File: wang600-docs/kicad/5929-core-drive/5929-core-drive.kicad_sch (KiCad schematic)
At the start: 29 parts, among them U17 7400

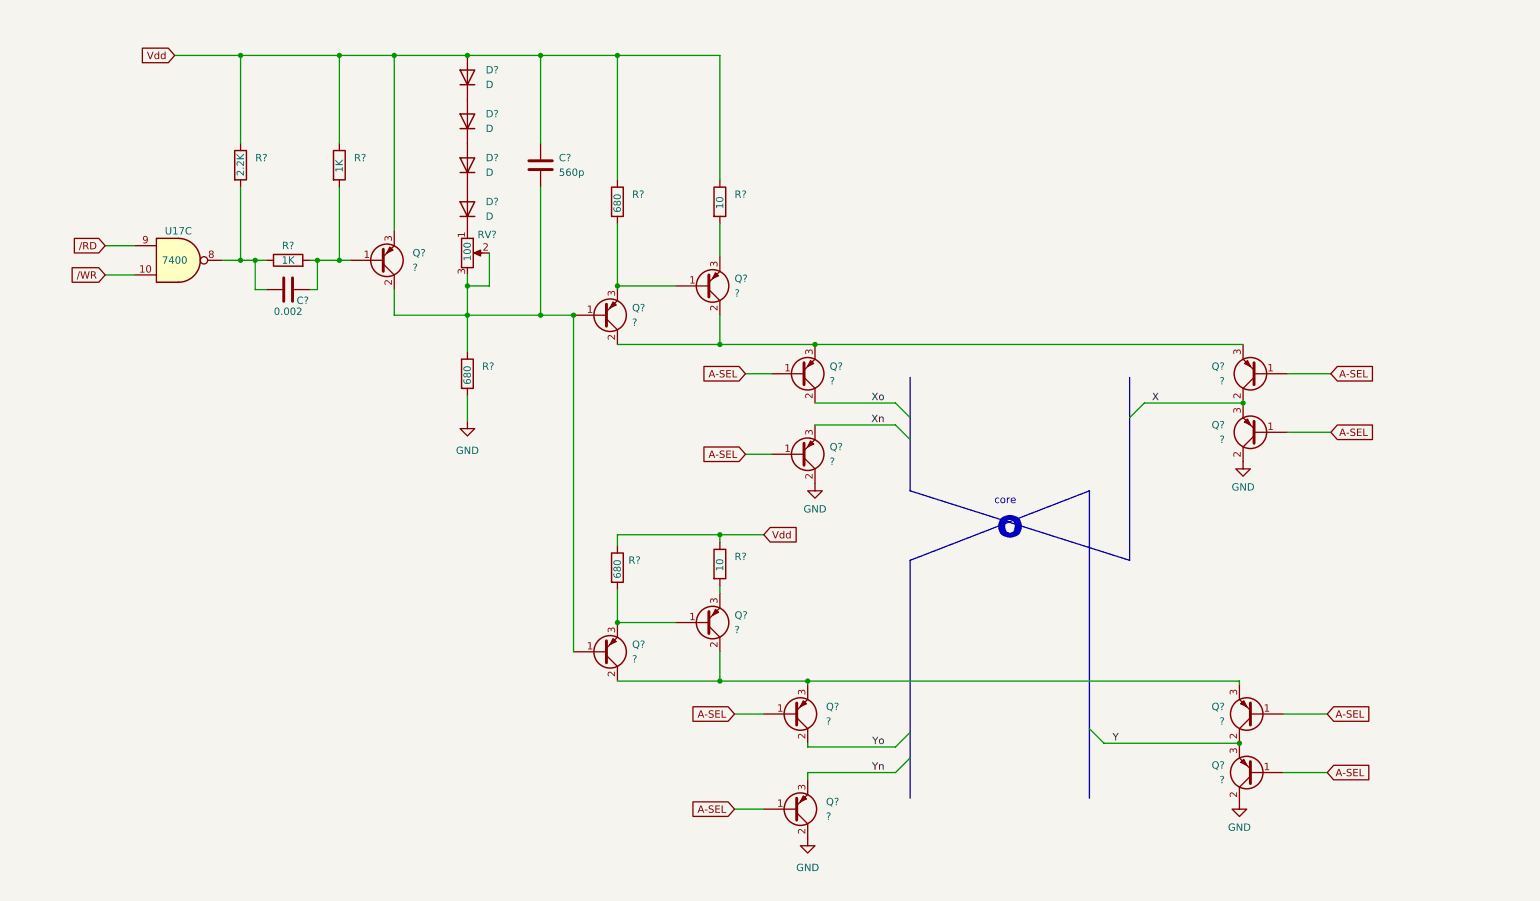
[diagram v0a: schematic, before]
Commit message: add transistor data to schematic
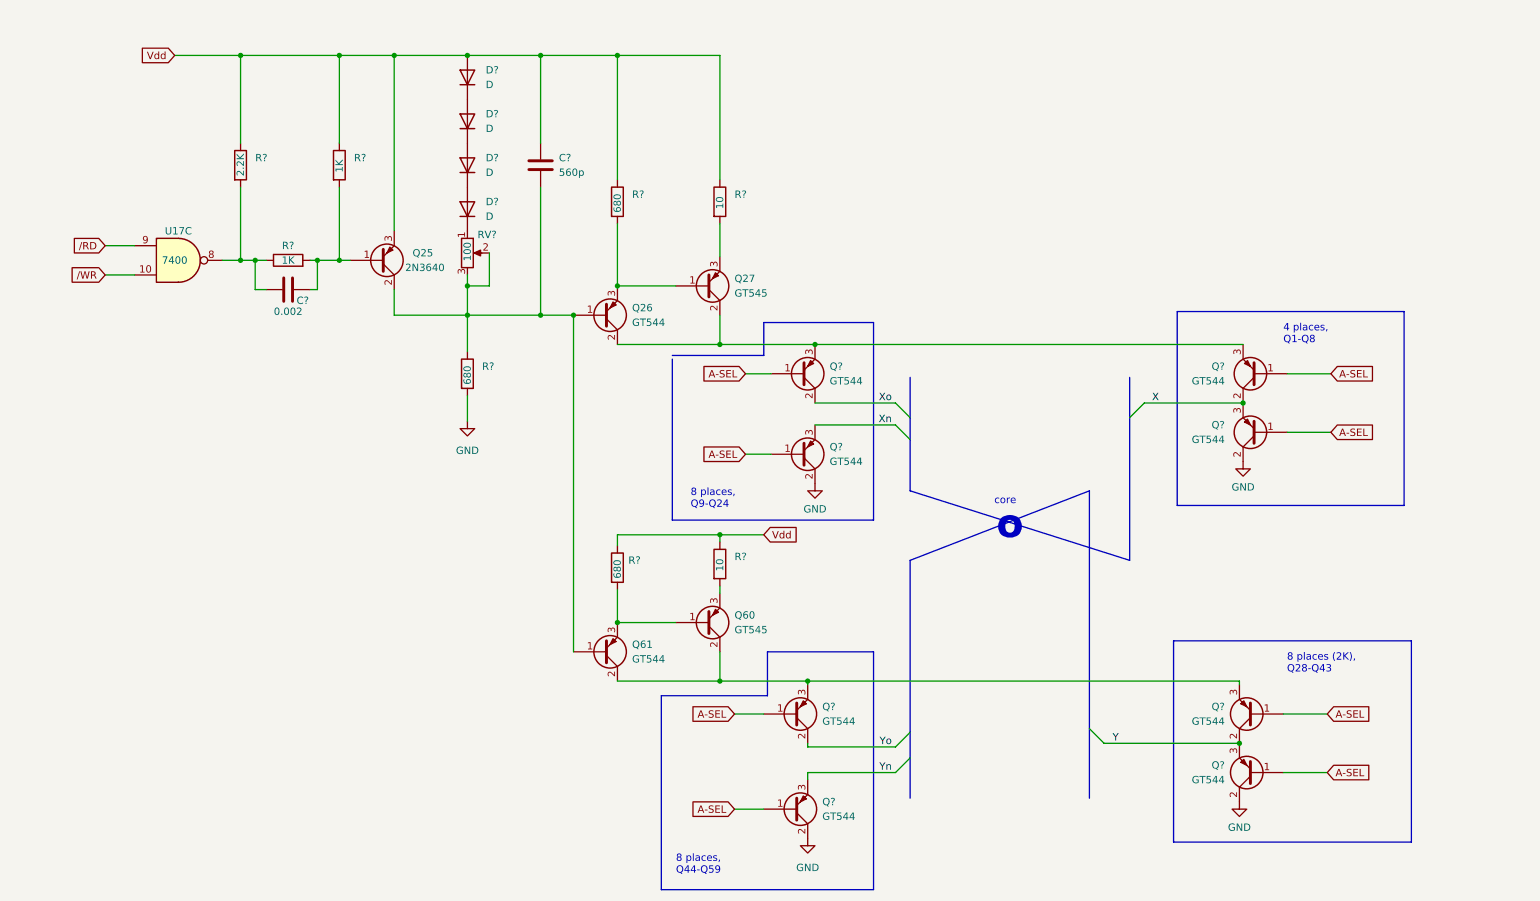
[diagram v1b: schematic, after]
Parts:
- Q25: renamed from Q?; value ? -> 2N3640
- Q26, Q61: renamed from Q?; value ? -> GT544
- Q27, Q60: renamed from Q?; value ? -> GT545
- Q? (x8): value ? -> GT544
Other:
- note added: "4 places, Q1-Q8"
- note added: "8 places (2K), Q28-Q43"
- note added: "8 places, Q44-Q59"
- note added: "8 places, Q9-Q24"

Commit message: add partno xref, more detail to schematics
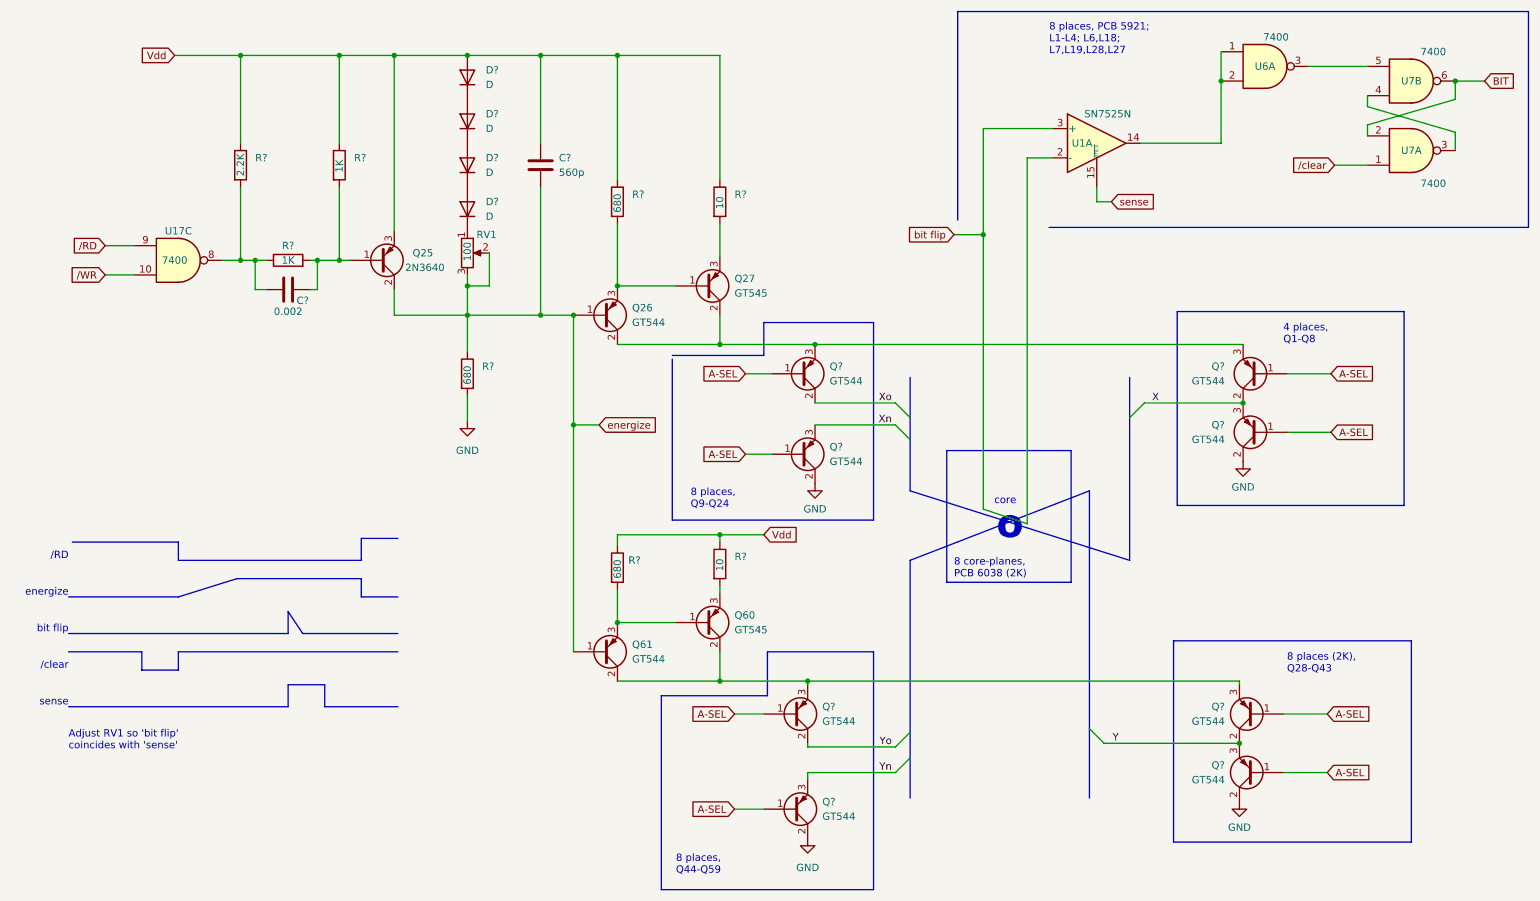
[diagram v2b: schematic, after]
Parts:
- added U1: SN7525N, Package_DFN_QFN:DFN-10-1EP_3x3mm_P0.5mm_EP1.55x2.48mm, symbol Amplifier_Operational:LTC6081xDD
- added U6, U7: 7400, symbol 74xx:74LS00
- gave numbers to parts that had none: 1
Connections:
- net energize: now reaches C?.2, Q25.2 (C), Q26.1 (B), Q61.1 (B), R?.1, RV1.2, RV1.3
- new net: U1.14, U6.1, U6.2
- new net: U6.3, U7.5
- new net: U7.3, U7.4
- new net BIT: U7.2, U7.6
- new net bit flip: U1.2 (-), U1.3 (+)
- new net sense: U1.15 (~{STB_A})
- new net /clear: U7.1
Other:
- note added: "/RD"
- note added: "/clear"
- note added: "8 core-planes, PCB 6038 (2K)"
- note added: "8 places, PCB 5921; L1-L4; L6,L18; L7,L19,L28,L27"
- note added: "Adjust RV1 so 'bit flip' coincides with 'sense'"
- note added: "bit flip"
- note added: "energize"
- note added: "sense"

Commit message: schematic cleanup
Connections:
- net A-SEL: no longer Q?.1 (B), Q?.1 (B), Q?.1 (B), Q?.1 (B)
- new net /A-SEL: Q?.1 (B), Q?.1 (B), Q?.1 (B), Q?.1 (B)
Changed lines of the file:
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@@
   (junction (at 94.615 26.67) (diameter 0) (color 0 0 0 0)
   )
-  (junction (at 184.15 57.785) (diameter 0) (color 0 0 0 0)
-  )
   (junction (at 94.615 71.755) (diameter 0) (color 0 0 0 0)
   )
@@
   (junction (at 81.915 26.67) (diameter 0) (color 0 0 0 0)
   )
+  (junction (at 184.15 62.865) (diameter 0) (color 0 0 0 0)
+  )
   (junction (at 68.58 62.23) (diameter 0) (color 0 0 0 0)
   )
@@
     (stroke (width 0) (type default) (color 0 0 0 0))
   )
-  (wire (pts (xy 184.15 39.37) (xy 184.15 57.785))
-    (stroke (width 0) (type default) (color 0 0 0 0))
-  )
-  (polyline (pts (xy 179.705 55.245) (xy 179.705 19.05))
+  (wire (pts (xy 184.15 39.37) (xy 184.15 62.865))
+    (stroke (width 0) (type default) (color 0 0 0 0))
+  )
+  (polyline (pts (xy 179.705 56.515) (xy 179.705 19.05))
     (stroke (width 0) (type default) (color 0 0 0 0))
   )
@@
     (stroke (width 0) (type default) (color 0 0 0 0))
   )
+  (wire (pts (xy 184.15 107.95) (xy 191.77 107.95))
+    (stroke (width 0) (type default) (color 0 0 0 0))
+  )
   (wire (pts (xy 153.67 135.255) (xy 153.67 135.89))
     (stroke (width 0) (type default) (color 0 0 0 0))
@@
     (stroke (width 0) (type default) (color 0 0 0 0))
   )
-  (wire (pts (xy 184.15 105.41) (xy 191.77 107.95))
-    (stroke (width 0) (type default) (color 0 0 0 0))
-  )
   (wire (pts (xy 236.22 151.13) (xy 243.84 151.13))
     (stroke (width 0) (type default) (color 0 0 0 0))
@@
     (stroke (width 0) (type default) (color 0 0 0 0))
   )
+  (wire (pts (xy 184.15 62.865) (xy 184.15 107.95))
+    (stroke (width 0) (type default) (color 0 0 0 0))
+  )
   (polyline (pts (xy 76.2 120.65) (xy 82.55 120.65))
     (stroke (width 0) (type solid) (color 0 0 194 1))
@@
     (stroke (width 0) (type default) (color 0 0 0 0))
   )
-  (wire (pts (xy 184.15 57.785) (xy 184.15 105.41))
+  (polyline (pts (xy 195.58 56.515) (xy 179.705 56.515))
     (stroke (width 0) (type default) (color 0 0 0 0))
   )
@@
     (stroke (width 0) (type solid) (color 0 0 194 1))
   )
-  (wire (pts (xy 179.07 57.785) (xy 184.15 57.785))
+  (wire (pts (xy 173.99 62.865) (xy 184.15 62.865))
     (stroke (width 0) (type default) (color 0 0 0 0))
   )
@@
     (stroke (width 0) (type default) (color 0 0 0 0))
   )
-  (text "8 places, PCB 5921;\nL1-L4; L6,L18;\nL7,L19,L28,L27" (at 195.58 26.67 0)
+  (text "8 places, PCB 5921;\nL1-L4; L6,L18;\nL7,L19,L28,L27" (at 180.975 26.67 0)
     (effects (font (size 1.27 1.27)) (justify left bottom))
   )
@@
     )
   )
-  (global_label "A-SEL" (shape input) (at 142.875 95.885 180) (fields_autoplaced)
+  (global_label "{slash}A-SEL" (shape input) (at 142.875 95.885 180) (fields_autoplaced)
     (effects (font (size 1.27 1.27)) (justify right))
-    (property "Intersheet References" "${INTERSHEET_REFS}" (id 0) (at 134.4143 95.8056 0)
+    (property "Intersheet References" "${INTERSHEET_REFS}" (id 0) (at 133.0838 95.8056 0)
       (effects (font (size 1.27 1.27)) (justify right) hide)
     )
@@
     )
   )
-  (global_label "A-SEL" (shape input) (at 140.97 157.48 180) (fields_autoplaced)
+  (global_label "{slash}A-SEL" (shape input) (at 140.97 157.48 180) (fields_autoplaced)
     (effects (font (size 1.27 1.27)) (justify right))
-    (property "Intersheet References" "${INTERSHEET_REFS}" (id 0) (at 132.5093 157.4006 0)
+    (property "Intersheet References" "${INTERSHEET_REFS}" (id 0) (at 131.1788 157.4006 0)
       (effects (font (size 1.27 1.27)) (justify right) hide)
     )
@@
     )
   )
-  (global_label "bit flip" (shape input) (at 179.07 57.785 180) (fields_autoplaced)
+  (global_label "bit flip" (shape input) (at 173.99 62.865 180) (fields_autoplaced)
     (effects (font (size 1.27 1.27)) (justify right))
-    (property "Intersheet References" "${INTERSHEET_REFS}" (id 0) (at 170.065 57.7056 0)
+    (property "Intersheet References" "${INTERSHEET_REFS}" (id 0) (at 164.985 62.7856 0)
       (effects (font (size 1.27 1.27)) (justify right) hide)
     )
   )
-  (global_label "A-SEL" (shape input) (at 244.475 81.915 0) (fields_autoplaced)
+  (global_label "{slash}A-SEL" (shape input) (at 244.475 81.915 0) (fields_autoplaced)
     (effects (font (size 1.27 1.27)) (justify left))
-    (property "Intersheet References" "${INTERSHEET_REFS}" (id 0) (at 252.9357 81.8356 0)
+    (property "Intersheet References" "${INTERSHEET_REFS}" (id 0) (at 254.2662 81.8356 0)
       (effects (font (size 1.27 1.27)) (justify left) hide)
     )
   )
-  (global_label "A-SEL" (shape input) (at 243.84 140.97 0) (fields_autoplaced)
+  (global_label "{slash}A-SEL" (shape input) (at 243.84 140.97 0) (fields_autoplaced)
     (effects (font (size 1.27 1.27)) (justify left))
-    (property "Intersheet References" "${INTERSHEET_REFS}" (id 0) (at 252.3007 140.8906 0)
+    (property "Intersheet References" "${INTERSHEET_REFS}" (id 0) (at 253.6312 140.8906 0)
       (effects (font (size 1.27 1.27)) (justify left) hide)
     )
@@
     )
     (pin "14")
+    (pin "15")
     (pin "2")
     (pin "3")
-    (pin "15")
   )
   (symbol (lib_id "Device:D") (at 94.615 38.1 90) (unit 1)

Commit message: cleanup schematics
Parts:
- added F?: core, symbol Z80-peripherals:Memory_Core
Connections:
- net bit flip: no longer U1.2 (-)
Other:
- note removed: "core"
- note removed: "o"
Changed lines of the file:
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@@
     (stroke (width 0) (type default) (color 0 0 0 0))
   )
-  (wire (pts (xy 191.77 44.45) (xy 191.77 107.95))
+  (wire (pts (xy 193.04 44.45) (xy 193.04 107.315))
     (stroke (width 0) (type default) (color 0 0 0 0))
   )
@@
     (stroke (width 0) (type default) (color 0 0 0 0))
   )
+  (wire (pts (xy 184.15 107.315) (xy 189.865 107.315))
+    (stroke (width 0) (type default) (color 0 0 0 0))
+  )
   (wire (pts (xy 228.6 135.89) (xy 228.6 135.255))
     (stroke (width 0) (type default) (color 0 0 0 0))
@@
     (stroke (width 0) (type default) (color 0 0 0 0))
   )
-  (wire (pts (xy 184.15 107.95) (xy 191.77 107.95))
-    (stroke (width 0) (type default) (color 0 0 0 0))
-  )
   (wire (pts (xy 153.67 135.255) (xy 153.67 135.89))
     (stroke (width 0) (type default) (color 0 0 0 0))
@@
     (stroke (width 0) (type default) (color 0 0 0 0))
   )
-  (bus (pts (xy 171.45 114.3) (xy 202.565 102.235))
+  (bus (pts (xy 171.45 114.3) (xy 189.865 106.68))
     (stroke (width 0) (type default) (color 0 0 0 0))
   )
@@
     (stroke (width 0) (type default) (color 0 0 0 0))
   )
-  (bus (pts (xy 171.45 102.235) (xy 209.55 114.3))
+  (bus (pts (xy 171.45 102.235) (xy 189.865 107.95))
     (stroke (width 0) (type default) (color 0 0 0 0))
   )
@@
     (stroke (width 0) (type default) (color 0 0 0 0))
   )
-  (wire (pts (xy 184.15 62.865) (xy 184.15 107.95))
+  (wire (pts (xy 184.15 62.865) (xy 184.15 107.315))
     (stroke (width 0) (type default) (color 0 0 0 0))
   )
@@
     (stroke (width 0) (type default) (color 0 0 0 0))
   )
+  (bus (pts (xy 192.405 108.585) (xy 209.55 114.3))
+    (stroke (width 0) (type default) (color 0 0 0 0))
+  )
   (wire (pts (xy 142.875 95.885) (xy 147.32 95.885))
     (stroke (width 0) (type default) (color 0 0 0 0))
   )
+  (bus (pts (xy 192.405 106.045) (xy 202.565 102.235))
+    (stroke (width 0) (type default) (color 0 0 0 0))
+  )
   (polyline (pts (xy 128.27 137.795) (xy 146.685 137.795))
     (stroke (width 0) (type default) (color 0 0 0 0))
@@
     (stroke (width 0) (type default) (color 0 0 0 0))
   )
-  (wire (pts (xy 196.215 44.45) (xy 191.77 44.45))
+  (wire (pts (xy 196.215 44.45) (xy 193.04 44.45))
     (stroke (width 0) (type default) (color 0 0 0 0))
   )
@@
   (polyline (pts (xy 69.85 135.89) (xy 69.85 139.7))
     (stroke (width 0) (type solid) (color 0 0 194 1))
+  )
+  (wire (pts (xy 192.405 107.315) (xy 193.04 107.315))
+    (stroke (width 0) (type default) (color 0 0 0 0))
   )
   (polyline (pts (xy 44.45 114.3) (xy 76.2 114.3))
@@
     (effects (font (size 1.27 1.27)) (justify right bottom))
   )
-  (text "core" (at 189.865 104.775 180)
-    (effects (font (size 1.27 1.27)) (justify right bottom))
-  )
   (text "sense" (at 25.4 139.7 180)
     (effects (font (size 1.27 1.27)) (justify right bottom))
@@
   (text "4 places,\nQ1-Q8" (at 236.22 76.835 0)
     (effects (font (size 1.27 1.27)) (justify left bottom))
-  )
-  (text "o" (at 191.135 111.125 180)
-    (effects (font (size 5 5) (thickness 1) bold) (justify right bottom))
   )
   (text "Adjust RV1 so 'bit flip'\ncoincides with 'sense'" (at 25.4 147.32 0)
@@
     (pin "3")
   )
+  (symbol (lib_id "Z80-peripherals:Memory_Core") (at 188.595 107.315 0) (unit 1)
+    (in_bom yes) (on_board yes)
+    (property "Reference" "F?" (id 0) (at 196.85 106.0449 0)
+      (effects (font (size 1.27 1.27)) (justify left) hide)
+    )
+    (property "Value" "core" (id 1) (at 186.69 102.235 0)
+      (effects (font (size 1.27 1.27)) (justify left))
+    )
+    (property "Footprint" "" (id 2) (at 188.595 107.315 0)
+      (effects (font (size 1.27 1.27)) hide)
+    )
+    (property "Datasheet" "" (id 3) (at 188.595 107.315 0)
+      (effects (font (size 1.27 1.27)) hide)
+    )
+  )
   (symbol (lib_id "Device:Q_PNP_BCE") (at 135.89 125.095 0) (mirror x) (unit 1)
     (in_bom yes) (on_board yes) (fields_autoplaced)
@@
       (reference "D?") (unit 1) (value "D") (footprint "")
     )
+    (path "/f68d1688-39d3-4df3-a31f-66904ee7037e"
+      (reference "F?") (unit 1) (value "core") (footprint "")
+    )
     (path "/a6b7df29-bcf8-46a9-b623-7eaac47f5110"
